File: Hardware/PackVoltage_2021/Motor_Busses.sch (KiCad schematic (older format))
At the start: 50 parts, among them Q1 PSMN025-80YL, Q2 PSMN025-80YL, Q3 PSMN025-80YL, Q4 PSMN025-80YL, Q5 PSMN025-80YL, U1 LT1910, U10 INA281, U2 LT1910, U3 LT1910, U4 INA281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

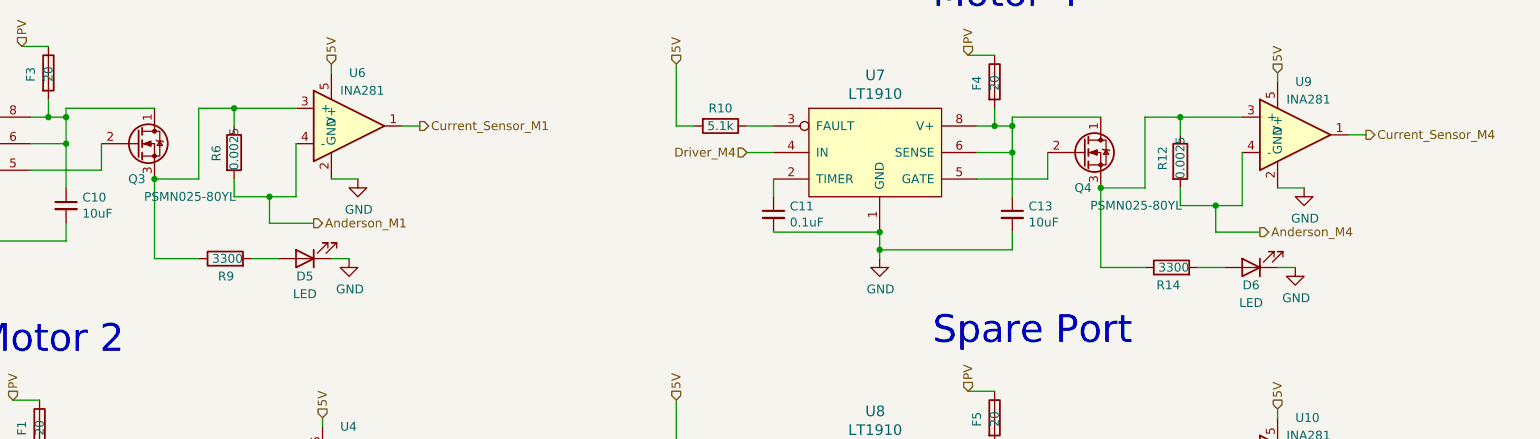
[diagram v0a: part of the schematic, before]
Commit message: changed mosfet footprint so its actually right
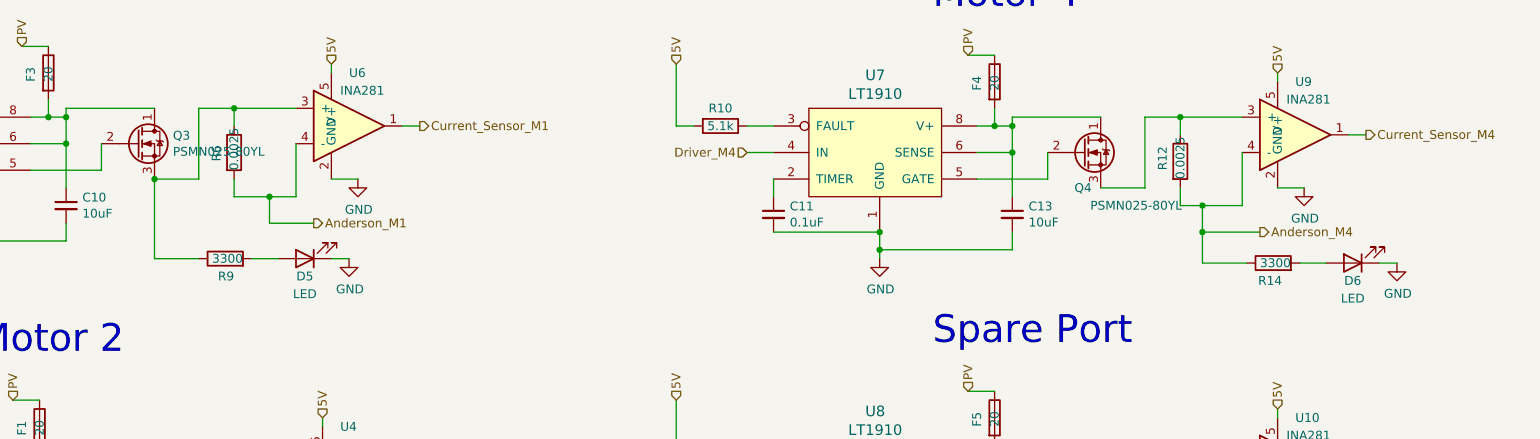
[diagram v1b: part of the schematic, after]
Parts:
- Q1, Q2, Q3, Q4, Q5: footprint Custom:LFPAK56_MOSFET -> Package_TO_SOT_SMD:LFPAK56
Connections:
- net Anderson_M4: now also R14.1
- net at Q4.3 (S), R12.1, U9.3 (+): no longer R14.1
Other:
- moved on the sheet: D6, R14
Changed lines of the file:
@@
 Motor Busses
-$Comp
-L Device:Q_NMOS_DGS Q3
-U 1 1 5F9AF789
-P 3000 1650
-AR Path="/5F7A6A8B/5F9AF789" Ref="Q3"  Part="1"
-AR Path="/5F8EFCC9/5F9AF789" Ref="Q?"  Part="1"
-F 0 "Q3" H 3000 1450 50  0000 C CNN
-F 1 "PSMN025-80YL" H 3300 1350 50  0000 C CNN
-F 2 "Custom:LFPAK56_MOSFET" H 3200 1750 50  0001 C CNN
-F 3 "~" H 3000 1650 50  0001 C CNN
-	1    3000 1650
-	1    0    0    -1
-$EndComp
 $Comp
 L power:GND #PWR018
@@
 	1    0    0    -1
 $EndComp
-Connection ~ 3100 1850
 Wire Wire Line
 	3550 1950 3750 1950
@@
 F 0 "Q1" H 2950 3450 50  0000 C CNN
 F 1 "PSMN025-80YL" H 3250 3350 50  0000 C CNN
-F 2 "Custom:LFPAK56_MOSFET" H 3150 3750 50  0001 C CNN
+F 2 "Package_TO_SOT_SMD:LFPAK56" H 3150 3750 50  0001 C CNN
 F 3 "~" H 2950 3650 50  0001 C CNN
 	1    2950 3650
@@
 F 0 "Q2" H 2950 5650 50  0000 C CNN
 F 1 "PSMN025-80YL" H 3250 5550 50  0000 C CNN
-F 2 "Custom:LFPAK56_MOSFET" H 3150 5950 50  0001 C CNN
+F 2 "Package_TO_SOT_SMD:LFPAK56" H 3150 5950 50  0001 C CNN
 F 3 "~" H 2950 5850 50  0001 C CNN
 	1    2950 5850
@@
 F 0 "Q4" H 8350 1500 50  0000 C CNN
 F 1 "PSMN025-80YL" H 8650 1400 50  0000 C CNN
-F 2 "Custom:LFPAK56_MOSFET" H 8550 1800 50  0001 C CNN
+F 2 "Package_TO_SOT_SMD:LFPAK56" H 8550 1800 50  0001 C CNN
 F 3 "~" H 8350 1700 50  0001 C CNN
 	1    8350 1700
@@
 L Device:LED D6
 U 1 1 5F9AF7B6
-P 9300 2350
+P 9875 2325
 AR Path="/5F7A6A8B/5F9AF7B6" Ref="D6"  Part="1"
 AR Path="/5F8EFCC9/5F9AF7B6" Ref="D?"  Part="1"
-F 0 "D6" H 9300 2450 50  0000 C CNN
-F 1 "LED" H 9300 2550 50  0000 C CNN
-F 2 "LED_SMD:LED_0603_1608Metric_Pad1.05x0.95mm_HandSolder" H 9300 2350 50  0001 C CNN
-F 3 "~" H 9300 2350 50  0001 C CNN
-	1    9300 2350
+F 0 "D6" H 9875 2425 50  0000 C CNN
+F 1 "LED" H 9875 2525 50  0000 C CNN
+F 2 "LED_SMD:LED_0603_1608Metric_Pad1.05x0.95mm_HandSolder" H 9875 2325 50  0001 C CNN
+F 3 "~" H 9875 2325 50  0001 C CNN
+	1    9875 2325
 	-1   0    0    1
 $EndComp
 Wire Wire Line
-	8450 2350 8700 2350
+	9025 2325 9275 2325
 $Comp
 L Device:R R14
 U 1 1 5F8B2B80
-P 8850 2350
+P 9425 2325
 AR Path="/5F7A6A8B/5F8B2B80" Ref="R14"  Part="1"
 AR Path="/5F8EFCC9/5F8B2B80" Ref="R?"  Part="1"
-F 0 "R14" V 8750 2300 50  0000 L CNN
-F 1 "3300" V 8850 2250 50  0000 L CNN
-F 2 "Resistor_SMD:R_0603_1608Metric_Pad1.05x0.95mm_HandSolder" V 8780 2350 50  0001 C CNN
-F 3 "~" H 8850 2350 50  0001 C CNN
-	1    8850 2350
+F 0 "R14" V 9325 2275 50  0000 L CNN
+F 1 "3300" V 9425 2225 50  0000 L CNN
+F 2 "Resistor_SMD:R_0603_1608Metric_Pad1.05x0.95mm_HandSolder" V 9355 2325 50  0001 C CNN
+F 3 "~" H 9425 2325 50  0001 C CNN
+	1    9425 2325
 	0    -1   -1   0
 $EndComp
 Wire Wire Line
-	9000 2350 9150 2350
-Wire Wire Line
-	9450 2350 9550 2350
+	9575 2325 9725 2325
+Wire Wire Line
+	10025 2325 10125 2325
 Text HLabel 7700 1150 1    50   Input ~ 0
 PV
@@
 L power:GND #PWR027
 U 1 1 5F8B2B9D
-P 9550 2350
+P 10125 2325
 AR Path="/5F7A6A8B/5F8B2B9D" Ref="#PWR027"  Part="1"
 AR Path="/5F8EFCC9/5F8B2B9D" Ref="#PWR?"  Part="1"
-F 0 "#PWR027" H 9550 2100 50  0001 C CNN
-F 1 "GND" H 9555 2177 50  0000 C CNN
-F 2 "" H 9550 2350 50  0001 C CNN
-F 3 "" H 9550 2350 50  0001 C CNN
-	1    9550 2350
-	1    0    0    -1
-$EndComp
-Connection ~ 8450 1900
-Wire Wire Line
-	8900 2000 9100 2000
-Wire Wire Line
-	9100 2150 9350 2150
+F 0 "#PWR027" H 10125 2075 50  0001 C CNN
+F 1 "GND" H 10130 2152 50  0000 C CNN
+F 2 "" H 10125 2325 50  0001 C CNN
+F 3 "" H 10125 2325 50  0001 C CNN
+	1    10125 2325
+	1    0    0    -1
+$EndComp
+Wire Wire Line
+	8900 2000 9025 2000
 Text HLabel 4000 2100 2    50   Output ~ 0
 Anderson_M1
@@
 F 0 "Q5" H 8350 3400 50  0000 C CNN
 F 1 "PSMN025-80YL" H 8650 3300 50  0000 C CNN
-F 2 "Custom:LFPAK56_MOSFET" H 8550 3700 50  0001 C CNN
+F 2 "Package_TO_SOT_SMD:LFPAK56" H 8550 3700 50  0001 C CNN
 F 3 "~" H 8350 3600 50  0001 C CNN
 	1    8350 3600
@@
 Wire Wire Line
 	9100 3900 9250 3900
-Wire Wire Line
-	8450 1900 8450 2350
-Wire Wire Line
-	9100 2150 9100 2000
-Connection ~ 9100 2000
-Wire Wire Line
-	9100 2000 9250 2000
 Text HLabel 9950 1600 2    50   Output ~ 0
 Current_Sensor_M4
@@
 Wire Wire Line
 	9450 4250 9550 4250
+Connection ~ 9025 2000
+Wire Wire Line
+	9025 2000 9025 2150
+Wire Wire Line
+	9025 2325 9025 2150
+Connection ~ 9025 2150
+Wire Wire Line
+	9025 2150 9350 2150
+Wire Wire Line
+	9025 2000 9250 2000
+Connection ~ 3100 1850
+$Comp
+L Device:Q_NMOS_DGS Q3
+U 1 1 5F9AF789
+P 3000 1650
+AR Path="/5F7A6A8B/5F9AF789" Ref="Q3"  Part="1"
+AR Path="/5F8EFCC9/5F9AF789" Ref="Q?"  Part="1"
+F 0 "Q3" H 3204 1696 50  0000 L CNN
+F 1 "PSMN025-80YL" H 3204 1605 50  0000 L CNN
+F 2 "Package_TO_SOT_SMD:LFPAK56" H 3200 1750 50  0001 C CNN
+F 3 "~" H 3000 1650 50  0001 C CNN
+	1    3000 1650
+	1    0    0    -1
+$EndComp
 $EndSCHEMATC

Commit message: updated mosfet footprints
but for real this time
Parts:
- Q1, Q2, Q3, Q4, Q5: value PSMN025-80YL -> BUK7M8R5-40HX; footprint Package_TO_SOT_SMD:LFPAK56 -> Package_TO_SOT_SMD:LFPAK33; symbol Device:Q_NMOS_DGS -> Transistor_FET:BUK9M24-40EX
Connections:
- net at Q3.3 (S), R6.1, R9.1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: now also Q3.1 (S), Q3.2 (S)
- net at C14.1, F5.2, U8.6 (SENSE)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: now also Q5.5 (D); no longer Q5.1 (D)
- net at Q5.2 (S): now also Q5.1 (S), Q5.3 (S), R13.1, R15.1, U10.3 (+); no longer U8.5 (GATE)
- net at C8.1, F1.2, U1.6 (SENSE)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: now also Q1.5 (D); no longer Q1.1 (D)
- net at Q1.2 (S): now also Q1.1 (S), Q1.3 (S), R4.1, R7.1, U4.3 (+); no longer U1.5 (GATE)
- net at C9.1, F2.2, U2.6 (SENSE)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: now also Q2.5 (D); no longer Q2.1 (D)
- net at Q2.2 (S): now also Q2.1 (S), Q2.3 (S), R5.1, R8.1, U5.3 (+); no longer U2.5 (GATE)
- net at Q4.3 (S), R12.1, U9.3 (+): now also Q4.1 (S), Q4.2 (S)
- net at U7.5 (GATE): now also Q4.4 (G); no longer Q4.2 (G)
- net at C13.1, F4.2, U7.6 (SENSE)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: now also Q4.5 (D); no longer Q4.1 (D)
- net at C10.1, F3.2, U3.6 (SENSE)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: now also Q3.5 (D); no longer Q3.1 (D)
- net at U3.5 (GATE): now also Q3.4 (G); no longer Q3.2 (G)
- new net: Q5.4 (G), U8.5 (GATE)
- new net: Q1.4 (G), U1.5 (GATE)
- new net: Q2.4 (G), U2.5 (GATE)

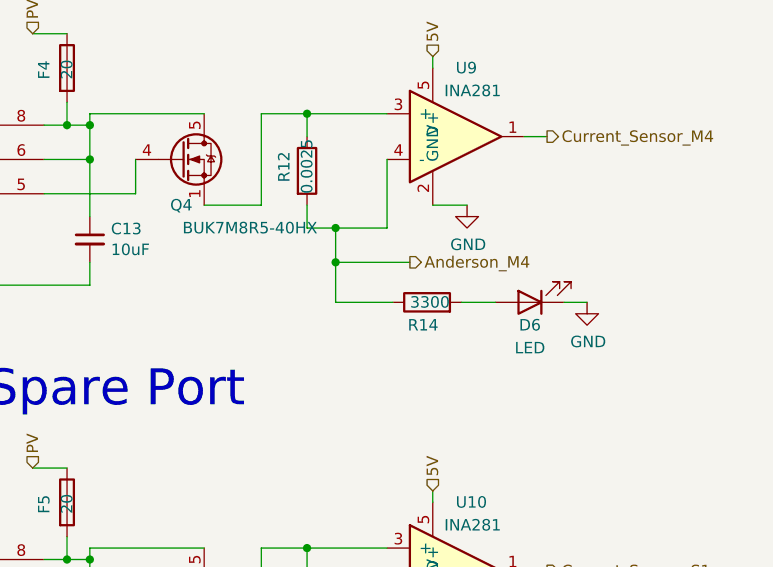
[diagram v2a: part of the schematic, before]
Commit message: uhh more circuits
finished top circuits on layout, fixed two resistors in schematic
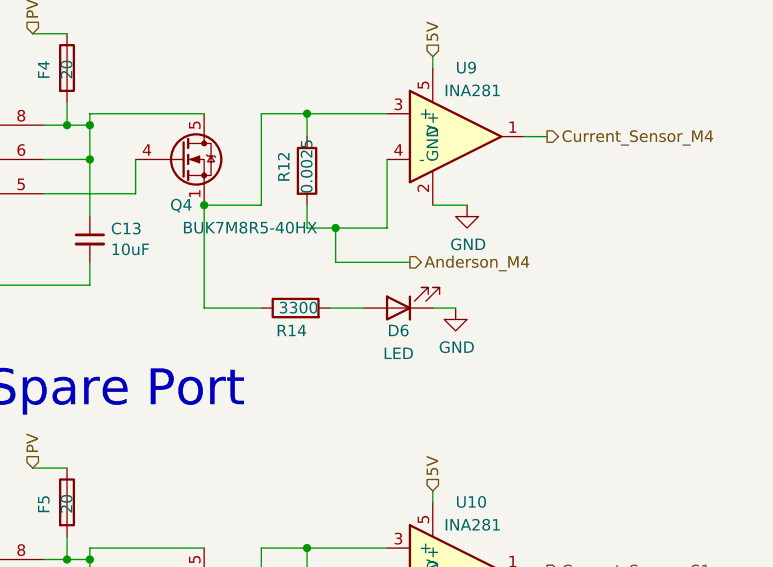
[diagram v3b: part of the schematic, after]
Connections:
- net Anderson_M4: no longer R14.1
- net at Q4.1 (S), Q4.2 (S), Q4.3 (S)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: now also R14.1
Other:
- moved on the sheet: D6, R14
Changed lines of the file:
@@
 	9450 1900 9600 1900
 Wire Wire Line
-	9025 2325 9275 2325
-Wire Wire Line
-	9575 2325 9725 2325
-Wire Wire Line
-	10025 2325 10125 2325
+	8450 2350 8700 2350
+Wire Wire Line
+	9000 2350 9150 2350
+Wire Wire Line
+	9450 2350 9550 2350
 Text HLabel 7700 1150 1    50   Input ~ 0
 PV
@@
 Wire Wire Line
 	9025 2000 9025 2150
-Wire Wire Line
-	9025 2325 9025 2150
-Connection ~ 9025 2150
 Wire Wire Line
 	9025 2150 9350 2150
@@
 L power:GND #PWR027
 U 1 1 5F8B2B9D
-P 10125 2325
+P 9550 2350
 AR Path="/5F7A6A8B/5F8B2B9D" Ref="#PWR027"  Part="1"
 AR Path="/5F8EFCC9/5F8B2B9D" Ref="#PWR?"  Part="1"
-F 0 "#PWR027" H 10125 2075 50  0001 C CNN
-F 1 "GND" H 10130 2152 50  0000 C CNN
-F 2 "" H 10125 2325 50  0001 C CNN
-F 3 "" H 10125 2325 50  0001 C CNN
-	1    10125 2325
+F 0 "#PWR027" H 9550 2100 50  0001 C CNN
+F 1 "GND" H 9555 2177 50  0000 C CNN
+F 2 "" H 9550 2350 50  0001 C CNN
+F 3 "" H 9550 2350 50  0001 C CNN
+	1    9550 2350
 	1    0    0    -1
 $EndComp
@@
 L Device:R R14
 U 1 1 5F8B2B80
-P 9425 2325
+P 8850 2350
 AR Path="/5F7A6A8B/5F8B2B80" Ref="R14"  Part="1"
 AR Path="/5F8EFCC9/5F8B2B80" Ref="R?"  Part="1"
-F 0 "R14" V 9325 2275 50  0000 L CNN
-F 1 "3300" V 9425 2225 50  0000 L CNN
-F 2 "Resistor_SMD:R_0603_1608Metric_Pad1.05x0.95mm_HandSolder" V 9355 2325 50  0001 C CNN
-F 3 "~" H 9425 2325 50  0001 C CNN
-	1    9425 2325
+F 0 "R14" V 8750 2300 50  0000 L CNN
+F 1 "3300" V 8850 2250 50  0000 L CNN
+F 2 "Resistor_SMD:R_0603_1608Metric_Pad1.05x0.95mm_HandSolder" V 8780 2350 50  0001 C CNN
+F 3 "~" H 8850 2350 50  0001 C CNN
+	1    8850 2350
 	0    -1   -1   0
 $EndComp
@@
 L Device:LED D6
 U 1 1 5F9AF7B6
-P 9875 2325
+P 9300 2350
 AR Path="/5F7A6A8B/5F9AF7B6" Ref="D6"  Part="1"
 AR Path="/5F8EFCC9/5F9AF7B6" Ref="D?"  Part="1"
-F 0 "D6" H 9875 2425 50  0000 C CNN
-F 1 "LED" H 9875 2525 50  0000 C CNN
-F 2 "LED_SMD:LED_0603_1608Metric_Pad1.05x0.95mm_HandSolder" H 9875 2325 50  0001 C CNN
-F 3 "~" H 9875 2325 50  0001 C CNN
-	1    9875 2325
+F 0 "D6" H 9300 2450 50  0000 C CNN
+F 1 "LED" H 9300 2550 50  0000 C CNN
+F 2 "LED_SMD:LED_0603_1608Metric_Pad1.05x0.95mm_HandSolder" H 9300 2350 50  0001 C CNN
+F 3 "~" H 9300 2350 50  0001 C CNN
+	1    9300 2350
 	-1   0    0    1
 $EndComp
@@
 	1    0    0    -1
 $EndComp
+Wire Wire Line
+	8450 1900 8450 2350
+Connection ~ 8450 1900
 $EndSCHEMATC
